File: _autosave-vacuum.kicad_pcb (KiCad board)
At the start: 2 copper layers, 67 parts, among them J1 к БП, J10 геркон шибера 1, J11 запасной, J12 запасной, J13 к БП, J2 нагрузка, J3 нагрузка, J4 геркон клапана 0, J5 нагрузка, J6 нагрузка, J7 к БП, J8 геркон клапана 1, J9 геркон шибера 0, Q1 IRF740, Q2 IRF740, Q3 IRF740, Q4 IRF740, SW1 Кнопка, SW2 Кнопка, SW3 Кнопка, SW4 Выключить автоматику, SW5 Кнопка, U1 PC817, U10 PC817, U2 PC817, U3 PC817, U4 PC817, U5 PC817, U6 PC817, U7 PC817, U8 PC817, U9 PC817

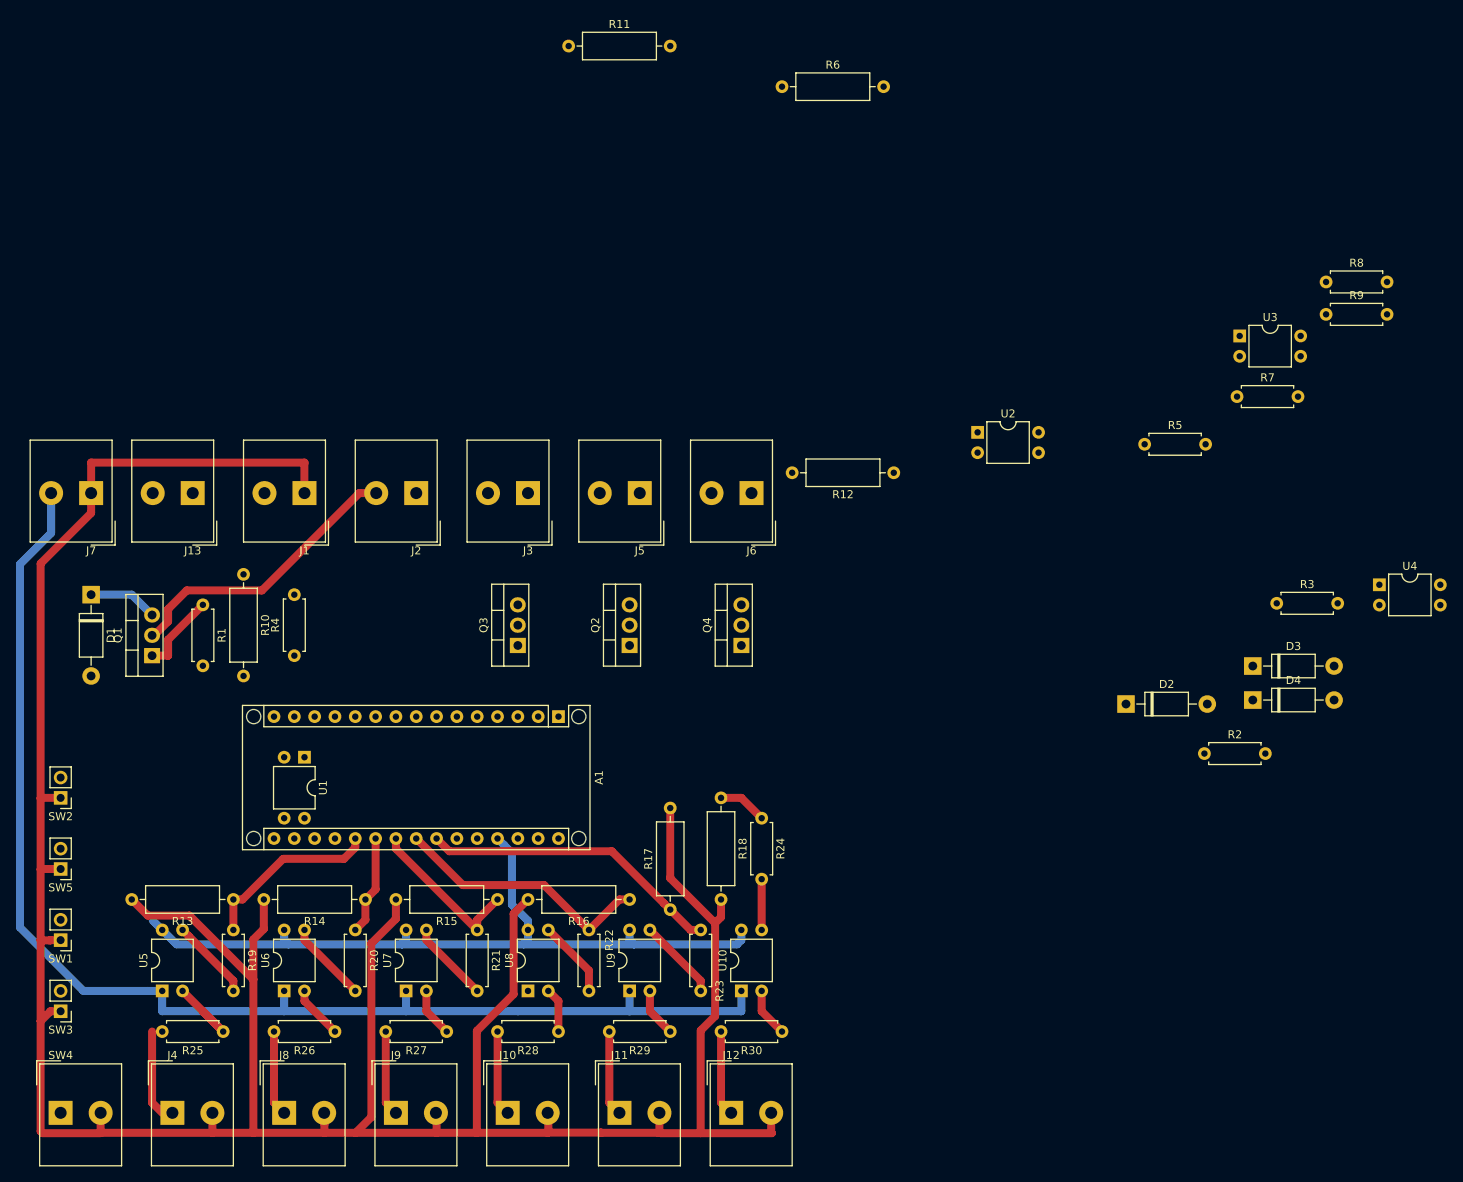
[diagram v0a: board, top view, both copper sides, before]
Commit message: some important bags in *.sch removed, PCB partially created
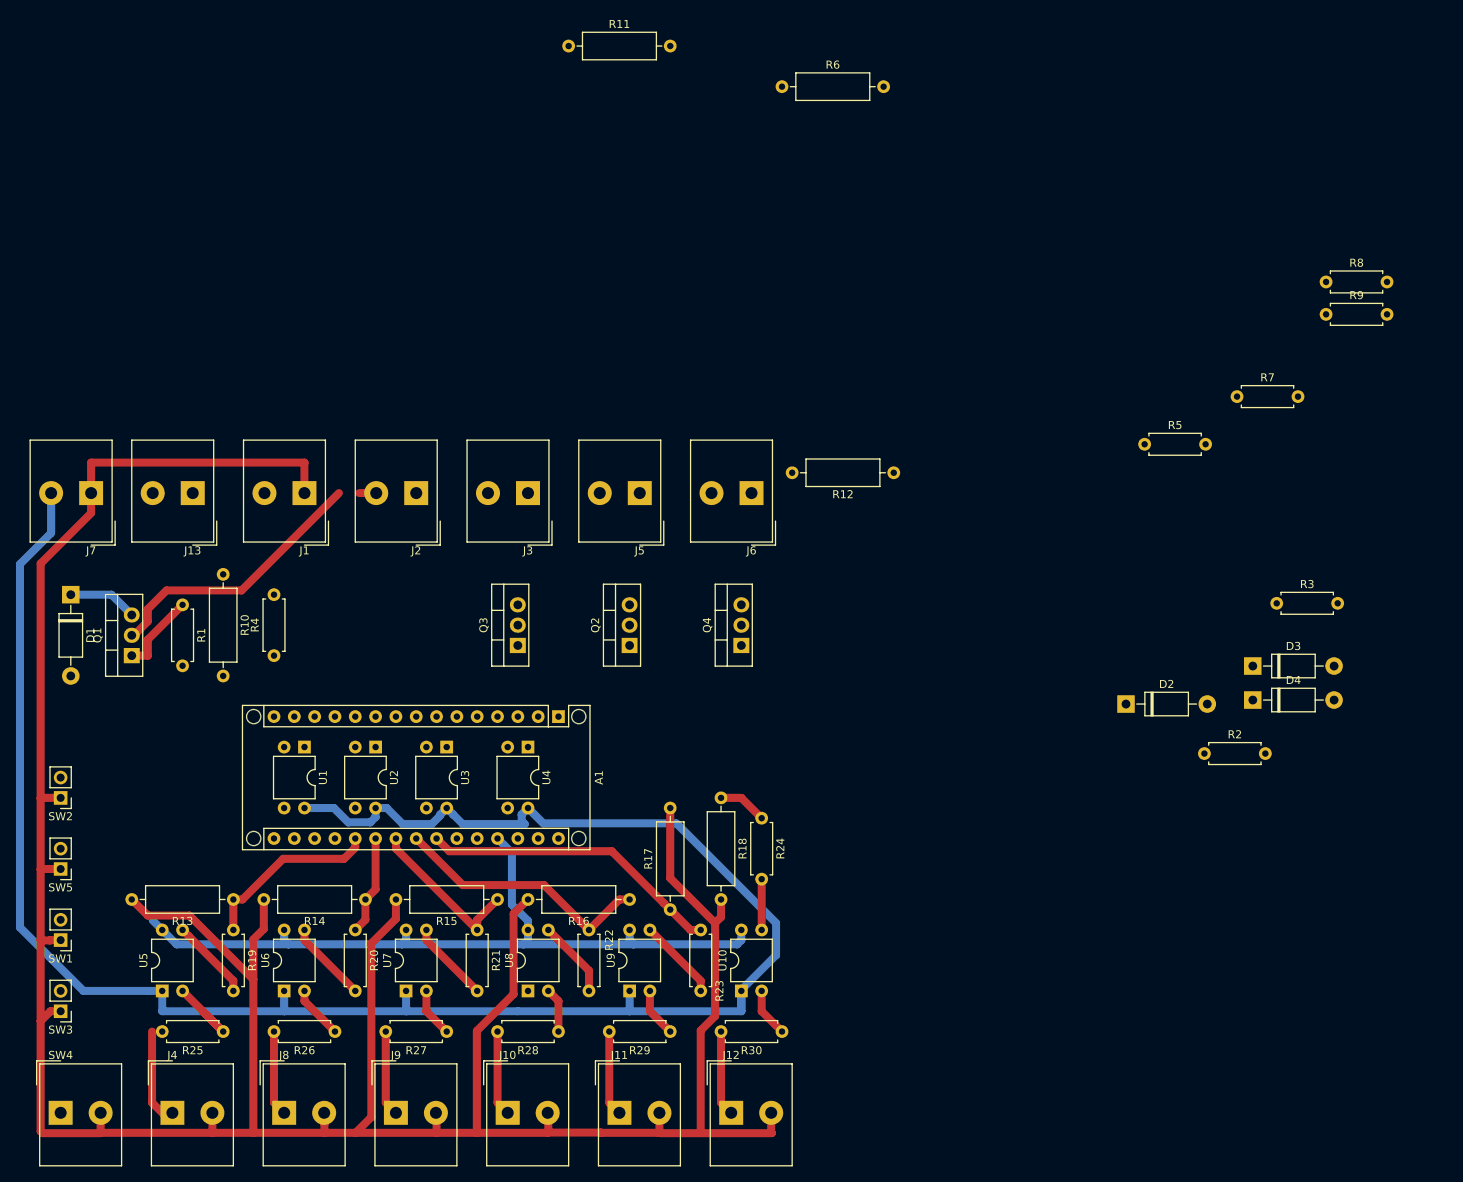
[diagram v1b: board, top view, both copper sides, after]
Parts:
- moved U3 111.6 mm to (115.6, 111.8), turned to 270 degrees
- moved U4 108.3 mm to (125.7, 111.8), turned to 270 degrees
- moved U2 84.9 mm to (106.7, 111.8), turned to 270 degrees
- moved D1 2.54 mm to (68.6, 92.7)
- moved R1 2.54 mm to (82.5, 94.0)
- moved R10 2.54 mm to (87.6, 90.2)
- moved Q1 2.54 mm to (76.2, 100.3)
- moved R4 2.54 mm to (94.0, 100.3)
- moved U1 1.27 mm to (97.8, 111.8)
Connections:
- U1 pad 3: +5V -> (no net)
- U2 pad 3: +5V -> (no net)
- U3 pad 3: +5V -> (no net)
- U4 pad 3: +5V -> (no net)
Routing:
- net +5V: track 162.1 -> 246.6 mm
